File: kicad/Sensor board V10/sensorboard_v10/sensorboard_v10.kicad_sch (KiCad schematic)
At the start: 28 parts, among them J1 Conn_01x02, J2 Conn_01x02, J3 Conn_01x04, J4 Conn_01x04, J5 Conn_01x04, J6 USB_C_Receptacle_USB2.0_14P, U1 ESP32-S3-WROOM-2, U2 LM2576S-5, U3 AMS1117-3.3, U4 TJA1051T-E, U5 CH340N

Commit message: Sensor Board V10
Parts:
- removed R18: 1k, symbol Device:R
- removed R19: 5k, symbol Device:R
- removed U4: TJA1051T-E, Package_SO:SOIC-8_3.9x4.9mm_P1.27mm, symbol Interface_CAN_LIN:TJA1051T-E
- removed U5: CH340N, Package_SO:SOP-8_3.9x4.9mm_P1.27mm, symbol Interface_USB:CH340N
- added C4, C5: 100nF, RMC_Capacitor:C_0805_2012Metric_Pad1.18x1.45mm_HandSolder_L, symbol Device:C
- added D1: D, Diode_SMD:D_SMA_Handsoldering, symbol Device:D
- added D3: LED, symbol Device:LED
- added F1, F2: Fuse, Fuse:Fuse_1210_3225Metric_Pad1.42x2.65mm_HandSolder, symbol Device:Fuse
- added H1, H2, H3, H4: MountingHole, MountingHole:MountingHole_3.2mm_M3, symbol Mechanical:MountingHole
- added J1: Conn_01x02, Connector_JST:JST_VH_B2P-VH_1x02_P3.96mm_Vertical, symbol Connector_Generic:Conn_01x02
- added Q1, Q2: MMBT3904, Package_TO_SOT_SMD:SOT-23_Handsoldering, symbol Transistor_BJT:MMBT3904
- added R23: 499R, RMC_Resistor:R_0805_2012Metric_Pad1.20x1.40mm_HandSolder_L, symbol Device:R
- added R4, R5: 10K, RMC_Resistor:R_0805_2012Metric_Pad1.20x1.40mm_HandSolder_L, symbol Device:R
- added R6: 120R, RMC_Resistor:R_0805_2012Metric_Pad1.20x1.40mm_HandSolder_L, symbol Device:R
- added SW1, SW2: SW_SPST, Button_Switch_THT:SW_PUSH_6mm_H5mm, symbol Switch:SW_SPST
- added U2: CH340C, Package_SO:SOIC-16_3.9x9.9mm_P1.27mm, symbol Interface_USB:CH340C
- added U3: TJA1051T-3, RMC_SO:SOIC-8_3.9x4.9mm_P1.27mm_RMC_Handsolder, symbol Interface_CAN_LIN:TJA1051T-3
- C1: renamed from C8; footprint (none) -> RMC_Capacitor:C_0805_2012Metric_Pad1.18x1.45mm_HandSolder_L
- C10: renamed from C6; footprint (none) -> RMC_Capacitor:C_0805_2012Metric_Pad1.18x1.45mm_HandSolder_L
- C11: renamed from C2; footprint (none) -> Capacitor_THT:CP_Radial_D6.3mm_P2.50mm
- C12: renamed from C4; value C -> 100nF; footprint (none) -> RMC_Capacitor:C_0805_2012Metric_Pad1.18x1.45mm_HandSolder_L
- C2: renamed from C9; footprint (none) -> RMC_Capacitor:C_0805_2012Metric_Pad1.18x1.45mm_HandSolder_L
- C3: renamed from C10; footprint (none) -> RMC_Capacitor:C_0805_2012Metric_Pad1.18x1.45mm_HandSolder_L
- C6: renamed from C3; footprint (none) -> RMC_Capacitor:C_0805_2012Metric_Pad1.18x1.45mm_HandSolder_L
- C7: renamed from C1; footprint (none) -> Capacitor_THT:CP_Radial_D6.3mm_P2.50mm
- C8: renamed from C7; footprint (none) -> RMC_Capacitor:C_0805_2012Metric_Pad1.18x1.45mm_HandSolder_L
- C9: renamed from C5; footprint (none) -> RMC_Capacitor:C_0805_2012Metric_Pad1.18x1.45mm_HandSolder_L
- D2: renamed from D1; footprint (none) -> Diode_SMD:D_SMA_Handsoldering
- J11: renamed from J2; footprint (none) -> Connector_JST:JST_XH_B2B-XH-A_1x02_P2.50mm_Vertical
- J2: renamed from J6; footprint Connector_USB:USB_C_Receptacle_GCT_USB4125-xx-x-0190_6P_TopMnt_Horizontal -> RMC_Connnector:USB_C_Receptacle_G-Switch_GT-USB-7010ASV_Handsolder
- J3: renamed from J1; footprint (none) -> Connector_JST:JST_VH_B2P-VH_1x02_P3.96mm_Vertical
- L1: footprint (none) -> RMC_Inductor:L_10.4x10.4_H4.8
- R1: renamed from R15; footprint (none) -> RMC_Resistor:R_0805_2012Metric_Pad1.20x1.40mm_HandSolder_L
- R2: renamed from R1; footprint (none) -> RMC_Resistor:R_0805_2012Metric_Pad1.20x1.40mm_HandSolder_L
- R3: renamed from R2; footprint (none) -> RMC_Resistor:R_0805_2012Metric_Pad1.20x1.40mm_HandSolder_L
- U4: renamed from U2; footprint Package_TO_SOT_SMD:TO-263-5_TabPin3 -> RMC_TO:TO-263-5_TabPin3_Handsolder
- U5: renamed from U3; footprint Package_TO_SOT_SMD:SOT-223-3_TabPin2 -> RMC_SOT:SOT-223-3_TabPin2_Handsolder
- renumbered J5 to J10, J3 to J6, J4 to J7
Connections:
- net +12V: no longer C8.2, U5.3 (VI)
- net +3.3V: now also F1.1, U2.16 (VCC), U2.4 (V3), U3.5 (VIO); no longer C1.1, C10.1, C10.2, C11.1, C12.1, C2.1, C3.1, C6.1, C7.1, C8.1, C9.1, C9.2, D2.2 (A), J10.3 (Pin_3), J3.2 (Pin_2), J6.3 (Pin_3), J7.3 (Pin_3), R3.1, U1.1 (GND), U1.40 (GND), U1.41 (GND), U4.3 (GND), U4.5 (~{ON}/OFF), U5.1 (GND), U5.2 (VO)
- net +5V: now also C8.2, U5.3 (VI), D1.1 (K), D3.2 (A), F2.2, U3.3 (VCC); no longer C11.2, C12.2, J2.A4 (VBUS), J2.A9 (VBUS), J2.B4 (VBUS), J2.B9 (VBUS), L1.2, U4.4 (FB)
- net APPS_3.3V_OUT: now also U1.38 (IO2)
- net CAN+: now also R6.1, U3.7 (CANH)
- net CAN-: now also R6.2, U3.6 (CANL)
- net CAN_RX: now also U3.4 (RXD)
- net CAN_TX: now also U3.1 (TXD)
- net D+: now also U2.5 (UD+)
- net D-: now also U2.6 (UD-)
- net LVB_S: now also U1.15 (IO3)
- net USB_TX: now also U1.36 (RXD0/IO44), U2.2 (TXD)
- net IO0: now reaches U1.27 (IO0)
- net IO0: now also C4.1, Q2.3 (C), SW1.2 (B)
- net ESP_EN: now reaches U1.3 (EN)
- net ESP_EN: now also C5.1, Q1.3 (C), SW2.2 (B)
- net at U1.37 (TXD0/IO43): now also R23.2
- net APPS_5V_OUT: now reaches U1.39 (IO1)
- net POT1_OUT: now reaches U1.4 (IO4)
- net POT2_OUT: now reaches U1.5 (IO5)
- net POT3_OUT: now reaches U1.6 (IO6)
- net POT4_OUT: now reaches U1.7 (IO7)
- net GND: now reaches J2.A1 (GND), J2.A12 (GND), J2.B1 (GND), J2.B12 (GND)
- net GND: now also C1.1, C10.1, C11.1, C12.1, C2.1, C3.1, C6.1, C7.1, C8.1, C9.2, D2.2 (A), J10.3 (Pin_3), J2.S1 (SHIELD), J3.2 (Pin_2), J6.3 (Pin_3), J7.3 (Pin_3), R3.1, U1.1 (GND), U1.40 (GND), U1.41 (GND), U4.3 (GND), U4.5 (~{ON}/OFF), U5.1 (GND), C4.2, C5.2, J1.1 (Pin_1), SW1.1 (A), SW2.1 (A), U2.1 (GND), U3.2 (GND)
- new net: Q2.1 (B), R5.2
- new net: C10.2, C9.1, F1.2, U5.2 (VO)
- new net: Q1.1 (B), R4.1
- new net: C11.2, C12.2, F2.1, L1.2, U4.4 (FB)
- new net: D1.2 (A), J2.A4 (VBUS), J2.A9 (VBUS), J2.B4 (VBUS), J2.B9 (VBUS)
- new net +24V: J1.2 (Pin_2)
- new net DTR: Q2.2 (E), R4.2, U2.13 (~{DTR})
- new net RTS: Q1.2 (E), R5.1, U2.14 (~{RTS})
- new net USB_RX: R23.1, U2.3 (RXD)
- no-connect marks 0 -> 10
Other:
- added sheet current to voltage (current to voltage.kicad_sch)
- added sheet voltage divider_3V3 (voltage.kicad_sch)
- sheet voltage divider ports: added 2.5V OUTPUT, 5V_INPUT; removed none
- sheet voltage divider1 ports: added 2.5V OUTPUT, 5V_INPUT; removed none
- sheet voltage divider2 ports: added 2.5V OUTPUT, 5V_INPUT; removed none
- sheet voltage divider3 ports: added 2.5V OUTPUT, 5V_INPUT; removed none
- sheet voltage divider4 ports: added 2.5V OUTPUT, 5V_INPUT; removed none
- sheet voltage divider5 ports: added 2.5V OUTPUT, 5V_INPUT; removed none
- sheet voltage divider6 ports: added 2.5V OUTPUT, 5V_INPUT; removed none
- moved on the sheet: C3, J10, J2, J3, J6, J7, R1, R2, R3

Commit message: Sensor Board V10 schematics
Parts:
- added C20, C26, C27, C28, C29: 100nF, RMC_Capacitor:C_0805_2012Metric_Pad1.18x1.45mm_HandSolder_L, symbol Device:C
- added D4: LED, RMC_LED:LED_0805_2012Metric_Pad1.45x1.40mm_HandSolder, symbol Device:LED
- added J19: Conn_01x03, Connector_JST:JST_XH_B3B-XH-A_1x03_P2.50mm_Vertical, symbol Connector_Generic:Conn_01x03
- added J20: Conn_01x02, Connector_JST:JST_XH_B2B-XH-A_1x02_P2.50mm_Vertical, symbol Connector_Generic:Conn_01x02
- added J21: Conn_01x06, Connector_PinHeader_2.54mm:PinHeader_2x03_P2.54mm_Vertical, symbol Connector_Generic:Conn_01x06
- added R21, R22: 1k, RMC_Resistor:R_0805_2012Metric_Pad1.20x1.40mm_HandSolder_L, symbol Device:R
- added R36: 4k7, RMC_Resistor:R_0805_2012Metric_Pad1.20x1.40mm_HandSolder_L, symbol Device:R
- added R37: 100K, RMC_Resistor:R_0805_2012Metric_Pad1.20x1.40mm_HandSolder_L, symbol Device:R
- added R38: 330R, RMC_Resistor:R_0805_2012Metric_Pad1.20x1.40mm_HandSolder_L, symbol Device:R
- added R39: 120R, RMC_Resistor:R_0805_2012Metric_Pad1.20x1.40mm_HandSolder_L, symbol Device:R
- added U7: TXS0102DCU, Package_SO:VSSOP-8_2.3x2mm_P0.5mm, symbol Logic_LevelTranslator:TXS0102DCU
- D3: footprint (none) -> RMC_LED:LED_0805_2012Metric_Pad1.45x1.40mm_HandSolder
- U1: footprint RF_Module:ESP32-S3-WROOM-2 -> to be sorted:ESP32-WROOM-S3-2
- U2: footprint Package_SO:SOIC-16_3.9x9.9mm_P1.27mm -> RMC_SO:SOIC-16_3.9x9.9mm_P1.27mm_Handsolder
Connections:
- net +3.3V: now also C26.2, J19.3 (Pin_3), R36.1, R39.1, U7.3 (VCCA), U7.6 (OE)
- net +5V: now also C27.1, J20.2 (Pin_2), J21.2 (Pin_2), R38.1, U7.7 (VCCB); no longer D3.2 (A)
- net APPS_3.3IN: now also J19.1 (Pin_1), R21.1
- net APPS_3.3V_OUT: now also C20.2, R21.2, R22.2
- net BRAKE_OUT: now also U1.12 (IO8)
- net BRAKE_TEMP_OUT1: now also U1.8 (IO15)
- net BRAKE_TEMP_OUT2: now also U1.9 (IO16)
- net BRAKE_TEMP_OUT3: now also U1.10 (IO17)
- net BRAKE_TEMP_OUT4: now also U1.11 (IO18)
- net CAN_RX: now also U1.13 (USB_D-/IO19)
- net CAN_TX: now also U1.14 (USB_D+/IO20)
- net FLOW_OUT: now also U1.22 (IO14)
- net GND: now also D3.1 (K), C20.1, C26.1, C27.2, C28.2, C29.2, D4.1 (K), J19.2 (Pin_2), J21.6 (Pin_6), R22.1, R36.2, R37.2, U7.2 (GND)
- net LVB_S: now also U1.18 (IO10), C29.1; no longer U1.15 (IO3)
- net LVB_TEMP: now also U1.15 (IO3)
- net SCL: now also U1.31 (IO38), U7.8 (B1)
- net SDA: now also U1.23 (IO21), U7.1 (B2)
- net PUMP_THERMISTOR_IN: now reaches U1.17 (IO9)
- net PUMP_THERMISTOR_IN: now also C28.1, J20.1 (Pin_1), R37.1
- net MOSI: now reaches U1.19 (IO11)
- net MOSI: now also J21.4 (Pin_4)
- net SCK: now reaches U1.20 (IO12)
- net SCK: now also J21.3 (Pin_3)
- net MISO: now reaches U1.21 (IO13)
- net MISO: now also J21.1 (Pin_1)
- new net: D3.2 (A), R38.2
- new net: D4.2 (A), R39.2
- new net SCL_3V3: U7.5 (A1)
- new net SDA_3V3: U7.4 (A2)
- no-connect marks 10 -> 15
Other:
- removed sheet voltage divider_3V3
- moved on the sheet: D3, J10, J7, R1, R2, R23, R3

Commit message: Sensor Board v10
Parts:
- removed C20: 100nF, RMC_Capacitor:C_0805_2012Metric_Pad1.18x1.45mm_HandSolder_L, symbol Device:C
- removed J1: Conn_01x02, Connector_JST:JST_VH_B2P-VH_1x02_P3.96mm_Vertical, symbol Connector_Generic:Conn_01x02
- removed J19: Conn_01x03, Connector_JST:JST_XH_B3B-XH-A_1x03_P2.50mm_Vertical, symbol Connector_Generic:Conn_01x03
- removed J21: Conn_01x06, Connector_PinHeader_2.54mm:PinHeader_2x03_P2.54mm_Vertical, symbol Connector_Generic:Conn_01x06
- removed R21, R22: 1k, RMC_Resistor:R_0805_2012Metric_Pad1.20x1.40mm_HandSolder_L, symbol Device:R
- added C32, C33: 22uF, RMC_Capacitor:C_0805_2012Metric_Pad1.18x1.45mm_HandSolder_L, symbol Device:C_Polarized
- added C34, C35: 100nF, RMC_Capacitor:C_0805_2012Metric_Pad1.18x1.45mm_HandSolder_L, symbol Device:C
- added D5: SMA Diode, Diode_SMD:D_SMA_Handsoldering, symbol Device:D_Zener
- added J21, J22: Conn_01x02, Connector_JST:JST_XH_B2B-XH-A_1x02_P2.50mm_Vertical, symbol Connector_Generic:Conn_01x02
- added J23, J26, J27: Conn_01x03, Connector_JST:JST_XH_B3B-XH-A_1x03_P2.50mm_Vertical, symbol Connector_Generic:Conn_01x03
- added J24: Conn_01x01, Connector_PinHeader_2.54mm:PinHeader_1x01_P2.54mm_Vertical, symbol Connector_Generic:Conn_01x01
- added J25: Conn_01x04, Connector_JST:JST_XH_B4B-XH-A_1x04_P2.50mm_Vertical, symbol Connector_Generic:Conn_01x04
- added L2: 4.7-22uH, RMC_Inductor:L_10.4x10.4_H4.8, symbol Device:L
- added R40: 4k7, RMC_Resistor:R_0805_2012Metric_Pad1.20x1.40mm_HandSolder_L, symbol Device:R
- added R41, R42: 5k1, RMC_Resistor:R_0805_2012Metric_Pad1.20x1.40mm_HandSolder_L, symbol Device:R
- added R43: 499R, RMC_Resistor:R_0805_2012Metric_Pad1.20x1.40mm_HandSolder_L, symbol Device:R
- added R44: 680R, RMC_Resistor:R_0805_2012Metric_Pad1.20x1.40mm_HandSolder_L, symbol Device:R
- added U9: MT3608/SDB628, Package_TO_SOT_SMD:SOT-23-6_Handsoldering, symbol Regulator_Switching:MT3608
- R23: value 499R -> 249k
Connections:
- net MOSI is gone; now on net LVB_TEMP: U1.19 (IO11)
- net SCK is gone; now on net BRAKE_OUT: U1.20 (IO12)
- net +12V: now also C32.1, C34.2, L2.1, U9.4 (EN), U9.5 (IN)
- net +24V: now also R23.1, C33.1, C35.2, D5.2 (A)
- net +3.3V: now also J26.3 (Pin_3), J27.3 (Pin_3), R40.1
- net BRAKE_OUT: no longer U1.12 (IO8)
- net CAN+: now also J21.1 (Pin_1)
- net CAN-: now also J21.2 (Pin_2)
- net CAN_RX: now also U1.23 (IO21); no longer U1.13 (USB_D-/IO19)
- net CAN_TX: now also U1.31 (IO38); no longer U1.14 (USB_D+/IO20)
- net GND: now also J26.2 (Pin_2), J27.2 (Pin_2), R41.1, R42.2
- net LVB_TEMP: now also J27.1 (Pin_1); no longer U1.15 (IO3)
- net SCL: now also U7.1 (B2); no longer U1.31 (IO38), U7.8 (B1)
- net SCL_3V3: now also U1.17 (IO9), U7.4 (A2); no longer U7.5 (A1)
- net SDA: now also U7.8 (B1); no longer U1.23 (IO21), U7.1 (B2)
- net SDA_3V3: now also U1.12 (IO8), U7.5 (A1); no longer U7.4 (A2)
- net USB_RX: now also U1.37 (TXD0/IO43), R43.1; no longer R23.1, U2.3 (RXD)
- net IO46: now reaches U1.16 (IO46)
- net IO46: now also J24.1 (Pin_1)
- net IO47: now reaches U1.24 (IO47)
- net IO47: now also J23.1 (Pin_1)
- net IO48: now reaches U1.25 (IO48)
- net IO48: now also J23.2 (Pin_2)
- net IO45: now reaches U1.26 (IO45)
- net IO45: now also J23.3 (Pin_3)
- net IO39: now reaches U1.32 (MTCK/IO39)
- net IO39: now also J25.1 (Pin_1)
- net IO40: now reaches U1.33 (MTDO/IO40)
- net IO40: now also J25.2 (Pin_2)
- net IO41: now reaches U1.34 (MTDI/IO41)
- net IO41: now also J25.3 (Pin_3)
- net IO42: now reaches U1.35 (MTMS/IO42)
- net IO42: now also J25.4 (Pin_4)
- net at R23.2: now also R44.1, U9.3 (FB); no longer U1.37 (TXD0/IO43)
- net at J2.A5 (CC1): now also R41.2
- net at J2.B5 (CC2): now also R42.1
- net MISO renamed PUMP_THERM_IN
- net PUMP_THERM_IN: now also C28.1, J20.1 (Pin_1), R37.1
- removed net PUMP_THERMISTOR_IN: C28.1, J20.1 (Pin_1), R37.1, U1.17 (IO9)
- new net: D5.1 (K), L2.2, U9.1 (SW)
- new net: R43.2, U2.3 (RXD)
- new net GND2: C32.2, C33.2, C34.1, C35.1, R44.2, U9.2 (GND)
- new net IO19: J22.1 (Pin_1), U1.13 (USB_D-/IO19)
- new net IO20: J22.2 (Pin_2), U1.14 (USB_D+/IO20)
- new net Temp_sensor: J26.1 (Pin_1), R40.2, U1.15 (IO3)
- no-connect marks 15 -> 7
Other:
- removed sheet voltage divider
- removed sheet voltage divider1
- removed sheet voltage divider2
- removed sheet voltage divider3
- added sheet 3V3 divider4 (3V3 divider.kicad_sch)
- added sheet voltage divider10 (voltage.kicad_sch)
- added sheet voltage divider7 (voltage.kicad_sch)
- added sheet voltage divider8 (voltage.kicad_sch)
- added sheet voltage divider9 (voltage.kicad_sch)
- sheet voltage divider6: file voltage.kicad_sch -> 5V_divider_schmitt_trigger.kicad_sch
- moved on the sheet: C1, C10, C2, C26, C27, C28, C29, C3, C4, C5, C8, C9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

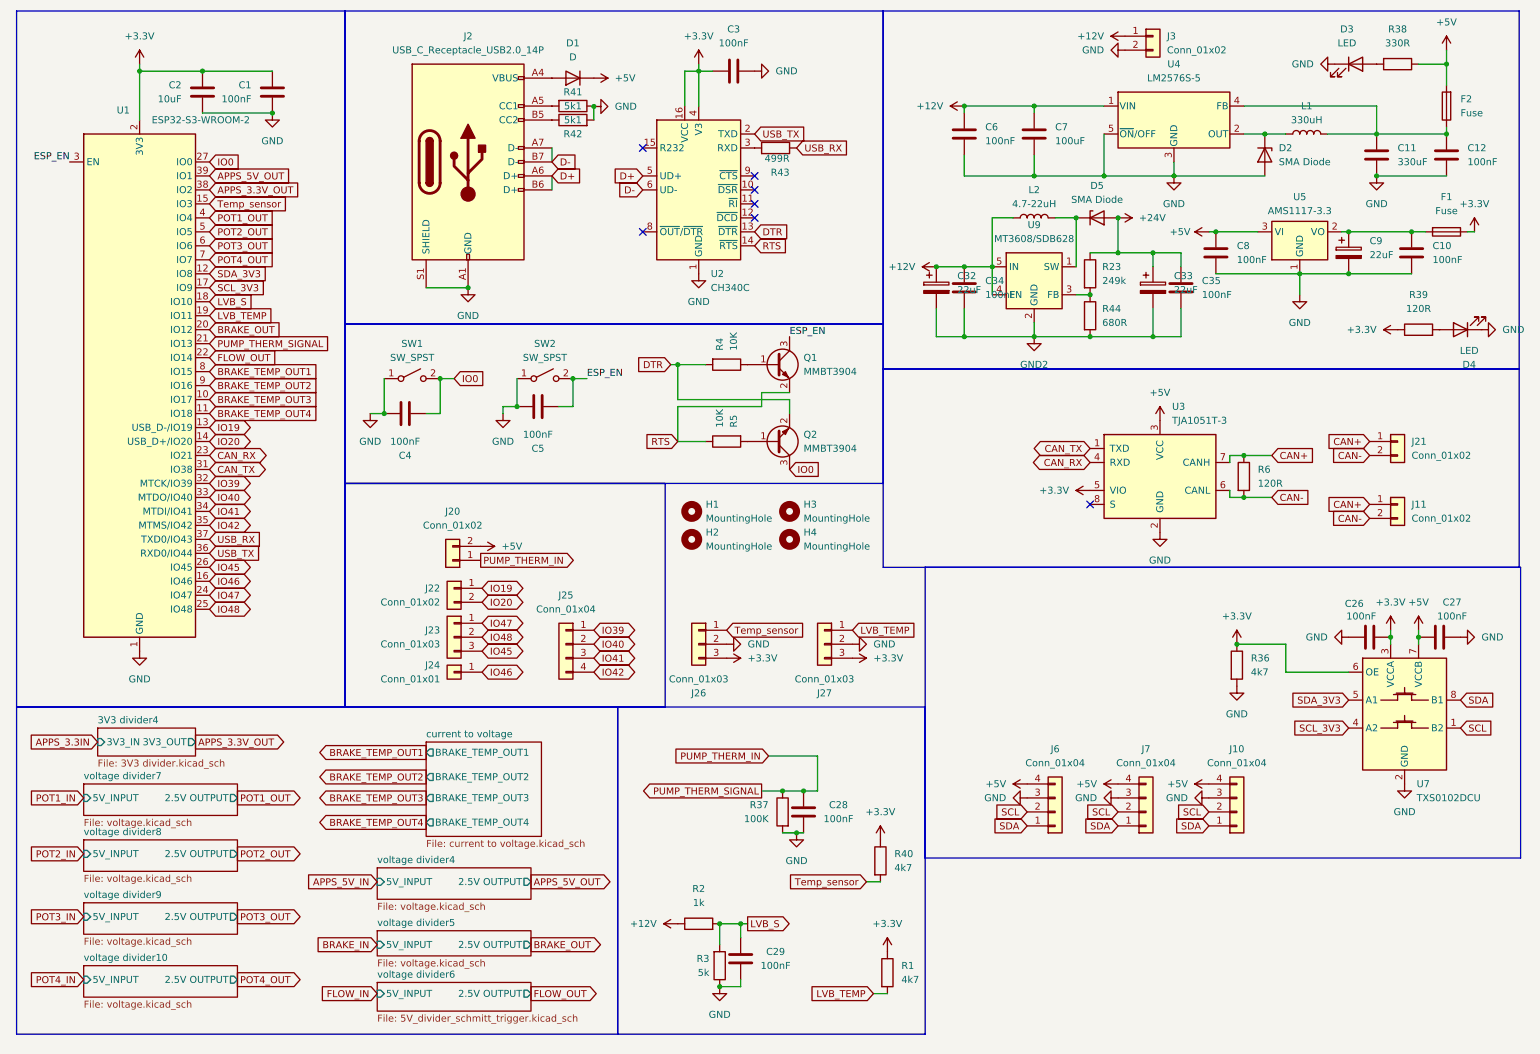
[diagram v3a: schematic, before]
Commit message: Sensor Board V10.0 done
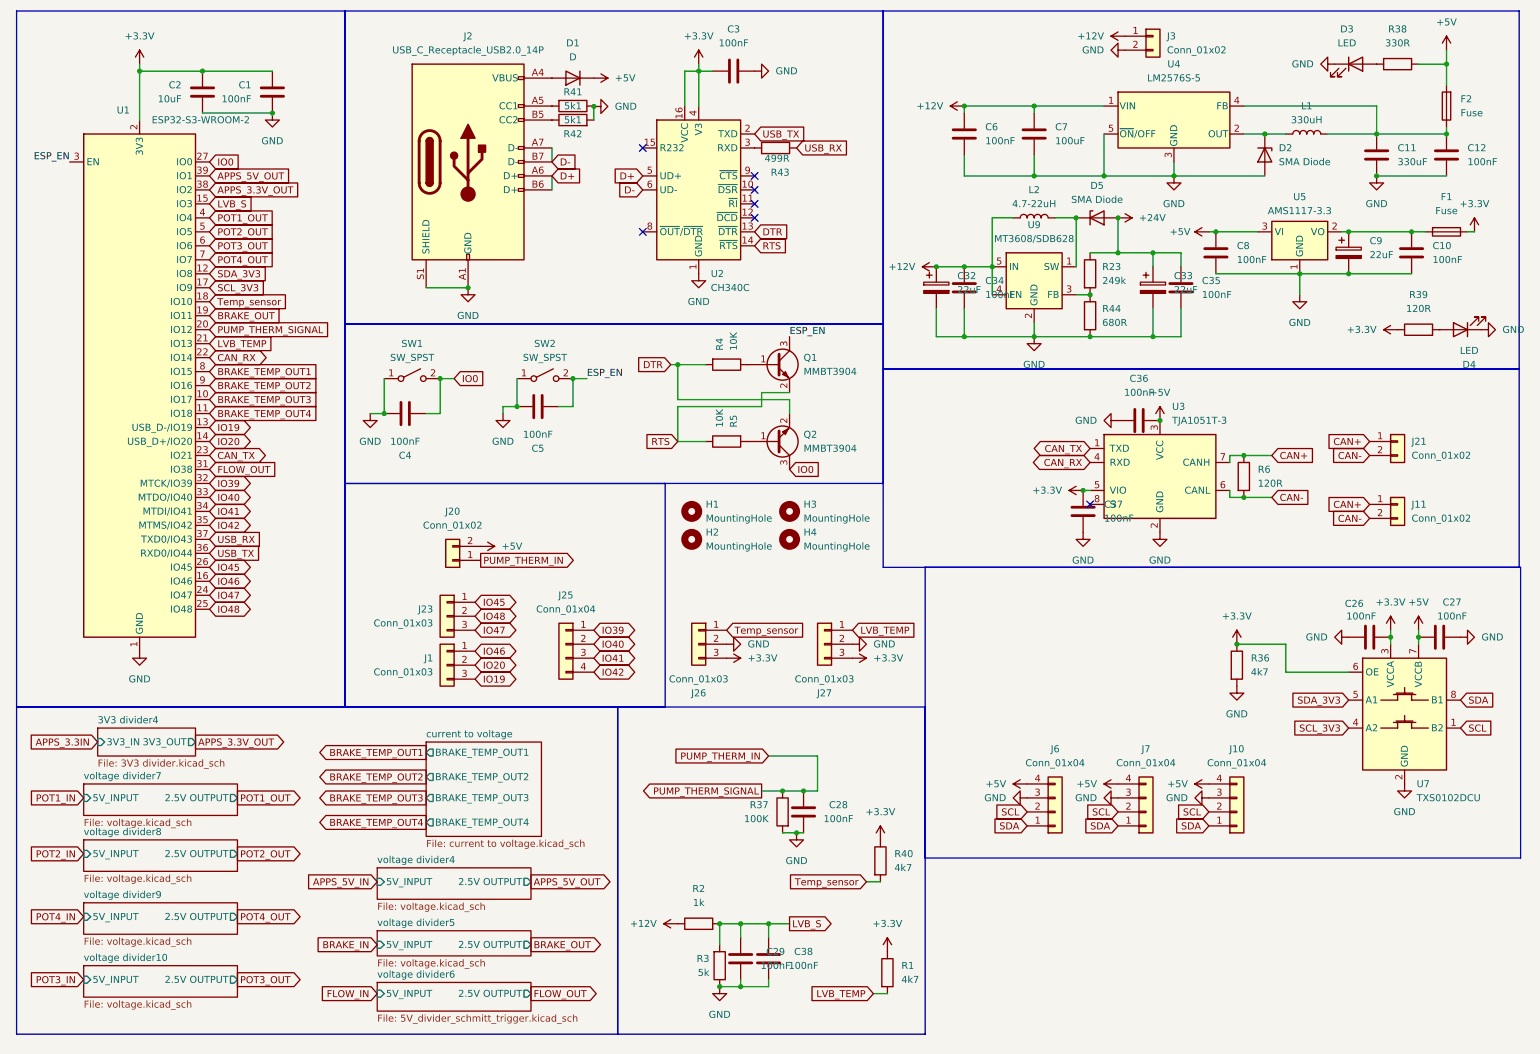
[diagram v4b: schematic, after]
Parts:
- removed J22: Conn_01x02, Connector_JST:JST_XH_B2B-XH-A_1x02_P2.50mm_Vertical, symbol Connector_Generic:Conn_01x02
- removed J24: Conn_01x01, Connector_PinHeader_2.54mm:PinHeader_1x01_P2.54mm_Vertical, symbol Connector_Generic:Conn_01x01
- added C36, C37, C38: 100nF, RMC_Capacitor:C_0805_2012Metric_Pad1.18x1.45mm_HandSolder_L, symbol Device:C
- added J1: Conn_01x03, Connector_JST:JST_XH_B3B-XH-A_1x03_P2.50mm_Vertical, symbol Connector_Generic:Conn_01x03
- L2: footprint RMC_Inductor:L_10.4x10.4_H4.8 -> Inductor_SMD:L_Wuerth_HCI-5040
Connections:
- net GND2 is gone; now on net GND: C32.2, C33.2, C34.1, C35.1, R44.2, U9.2 (GND)
- net +12V: now also C7.1; no longer C7.2
- net +3.3V: now also C37.2
- net +5V: now also C36.1
- net BRAKE_OUT: now also U1.19 (IO11); no longer U1.20 (IO12)
- net CAN_RX: now also U1.22 (IO14); no longer U1.23 (IO21)
- net CAN_TX: now also U1.23 (IO21); no longer U1.31 (IO38)
- net FLOW_OUT: now also U1.31 (IO38); no longer U1.22 (IO14)
- net GND: now also C11.2, C7.2, C36.2, C37.1, C38.2; no longer C11.1, C7.1
- net IO19: now also J1.3 (Pin_3)
- net IO20: now also J1.2 (Pin_2)
- net IO45: now also J23.1 (Pin_1); no longer J23.3 (Pin_3)
- net IO46: now also J1.1 (Pin_1)
- net IO47: now also J23.3 (Pin_3); no longer J23.1 (Pin_1)
- net LVB_S: now also U1.15 (IO3), C38.1; no longer U1.18 (IO10)
- net LVB_TEMP: now also U1.21 (IO13); no longer U1.19 (IO11)
- net PUMP_THERM_IN: now also U1.20 (IO12); no longer U1.21 (IO13)
- net Temp_sensor: now also U1.18 (IO10); no longer U1.15 (IO3)
- net at C12.2, F2.1, L1.2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: now also C11.1; no longer C11.2
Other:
- moved on the sheet: C11, C7, J23
